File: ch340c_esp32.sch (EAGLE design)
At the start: 13 parts, among them J1 CQ-USB-C16PSMT01, U1 AMS1117 3.3V, U2 CH340C, U3 AO3400, U4 AO3400

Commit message: prototype v1.1
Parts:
- added JP1: JUMPER-SMT_3_NO_NO-SILK, SparkFun-Jumpers:JUMPER-SMT_3_NO_NO-SILK
- C2: value 1uF -> 100nF
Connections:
- net DN1 renamed DN
- net DP1 renamed DP
- removed net NC.: U2.NC.
- removed net SBU1: J1.SBU1
- removed net SBU2: J1.SBU2
- removed net VIN: J1.VBUS, U1.VIN
- removed net VOUT: C1.1, U1.VOUT, U2.V3, U2.VCC
- new net 3V3: JP1.1, U1.VOUT
- new net 5V: J1.VBUS, JP1.3, U1.VIN
- new net V3: C1.1, U2.V3
- new net VCC: JP1.2, U2.VCC
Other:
- moved on the sheet: C1, C2, R1, R2

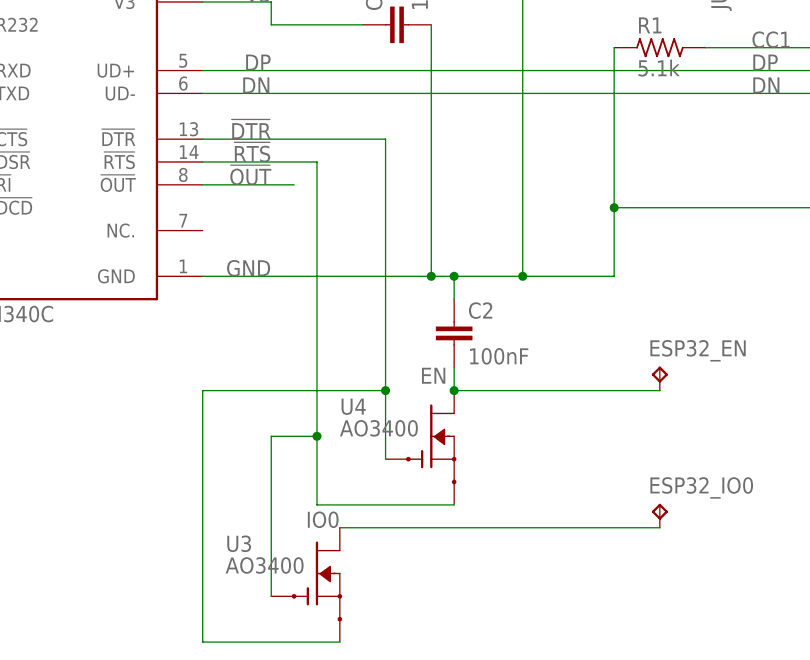
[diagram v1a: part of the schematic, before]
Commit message: update C2 cap value
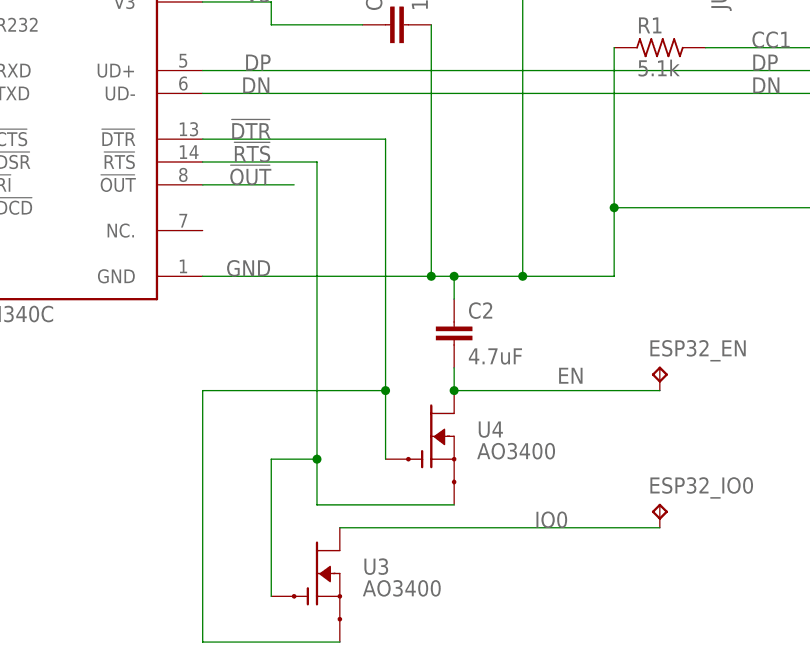
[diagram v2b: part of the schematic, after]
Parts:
- C2: value 100nF -> 4.7uF
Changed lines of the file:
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@@
 <setting verticaltext="up"/>
 </settings>
-<grid distance="0.1" unitdist="inch" unit="inch" style="dots" multiple="1" display="yes" altdistance="0.01" altunitdist="inch" altunit="inch"/>
+<grid distance="0.1" unitdist="inch" unit="inch" style="lines" multiple="1" display="no" altdistance="0.01" altunitdist="inch" altunit="inch"/>
 <layers>
 <layer number="1" name="Top" color="4" fill="1" visible="no" active="no"/>
@@
 <part name="ESP32_TX" library="BeagleBone_Blue_R3" library_urn="urn:adsk.eagle:library:5828899" deviceset="TP" device="B1,27" package3d_urn="urn:adsk.eagle:package:5829429/1"/>
 <part name="ESP32_RX" library="BeagleBone_Blue_R3" library_urn="urn:adsk.eagle:library:5828899" deviceset="TP" device="B1,27" package3d_urn="urn:adsk.eagle:package:5829429/1"/>
-<part name="C2" library="eagle-ltspice" library_urn="urn:adsk.eagle:library:217" deviceset="C" device="C0603" package3d_urn="urn:adsk.eagle:package:13262/1" value="100nF"/>
+<part name="C2" library="eagle-ltspice" library_urn="urn:adsk.eagle:library:217" deviceset="C" device="C0603" package3d_urn="urn:adsk.eagle:package:13262/1" value="4.7uF"/>
 <part name="JP1" library="SparkFun-Jumpers" library_urn="urn:adsk.eagle:library:528" deviceset="JUMPER-SMT_3_NO" device="_NO-SILK" package3d_urn="urn:adsk.eagle:package:39284/1" value="JUMPER-SMT_3_NO_NO-SILK"/>
 </parts>
@@
 </instance>
 <instance part="U3" gate="G$1" x="152.4" y="-12.7" smashed="yes">
-<attribute name="NAME" x="142.24" y="-10.287" size="1.778" layer="95"/>
-<attribute name="VALUE" x="142.24" y="-12.7" size="1.778" layer="96"/>
+<attribute name="NAME" x="157.48" y="-12.827" size="1.778" layer="95"/>
+<attribute name="VALUE" x="157.48" y="-15.24" size="1.778" layer="96"/>
 </instance>
 <instance part="U4" gate="G$1" x="165.1" y="2.54" smashed="yes">
-<attribute name="NAME" x="154.94" y="4.953" size="1.778" layer="95"/>
-<attribute name="VALUE" x="154.94" y="2.54" size="1.778" layer="96"/>
+<attribute name="NAME" x="170.18" y="2.413" size="1.778" layer="95"/>
+<attribute name="VALUE" x="170.18" y="0" size="1.778" layer="96"/>
 </instance>
 <instance part="ESP32_EN" gate="G$1" x="190.5" y="10.16" smashed="yes">
@@
 <wire x1="139.7" y1="33.02" x2="152.4" y2="33.02" width="0.1524" layer="91"/>
 <label x="147.32" y="33.02" size="1.778" layer="95" align="bottom-right"/>
-<wire x1="152.4" y1="33.02" x2="152.4" y2="2.54" width="0.1524" layer="91"/>
+<wire x1="152.4" y1="33.02" x2="152.4" y2="0" width="0.1524" layer="91"/>
 <pinref part="U3" gate="G$1" pin="G"/>
-<wire x1="147.32" y1="-15.24" x2="147.32" y2="2.54" width="0.1524" layer="91"/>
-<wire x1="147.32" y1="2.54" x2="152.4" y2="2.54" width="0.1524" layer="91"/>
+<wire x1="147.32" y1="-15.24" x2="147.32" y2="0" width="0.1524" layer="91"/>
+<wire x1="147.32" y1="0" x2="152.4" y2="0" width="0.1524" layer="91"/>
 <pinref part="U4" gate="G$1" pin="S"/>
 <wire x1="167.64" y1="-5.08" x2="152.4" y2="-5.08" width="0.1524" layer="91"/>
-<wire x1="152.4" y1="-5.08" x2="152.4" y2="2.54" width="0.1524" layer="91"/>
-<junction x="152.4" y="2.54"/>
+<wire x1="152.4" y1="-5.08" x2="152.4" y2="0" width="0.1524" layer="91"/>
+<junction x="152.4" y="0"/>
 </segment>
 </net>
@@
 <pinref part="U3" gate="G$1" pin="D"/>
 <wire x1="154.94" y1="-7.62" x2="190.5" y2="-7.62" width="0.1524" layer="91"/>
-<label x="154.94" y="-7.62" size="1.778" layer="95" align="bottom-right"/>
+<label x="180.34" y="-7.62" size="1.778" layer="95" align="bottom-right"/>
 <pinref part="ESP32_IO0" gate="G$1" pin="TP"/>
 </segment>
@@
 <segment>
 <pinref part="U4" gate="G$1" pin="D"/>
-<label x="166.878" y="8.382" size="1.778" layer="95" align="bottom-right"/>
+<label x="182.118" y="8.382" size="1.778" layer="95" align="bottom-right"/>
 <pinref part="C2" gate="G$1" pin="2"/>
 <junction x="167.64" y="7.62"/>
